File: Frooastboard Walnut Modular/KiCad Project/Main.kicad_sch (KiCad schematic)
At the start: 253 parts, among them M2 Frooastboard_MM2040

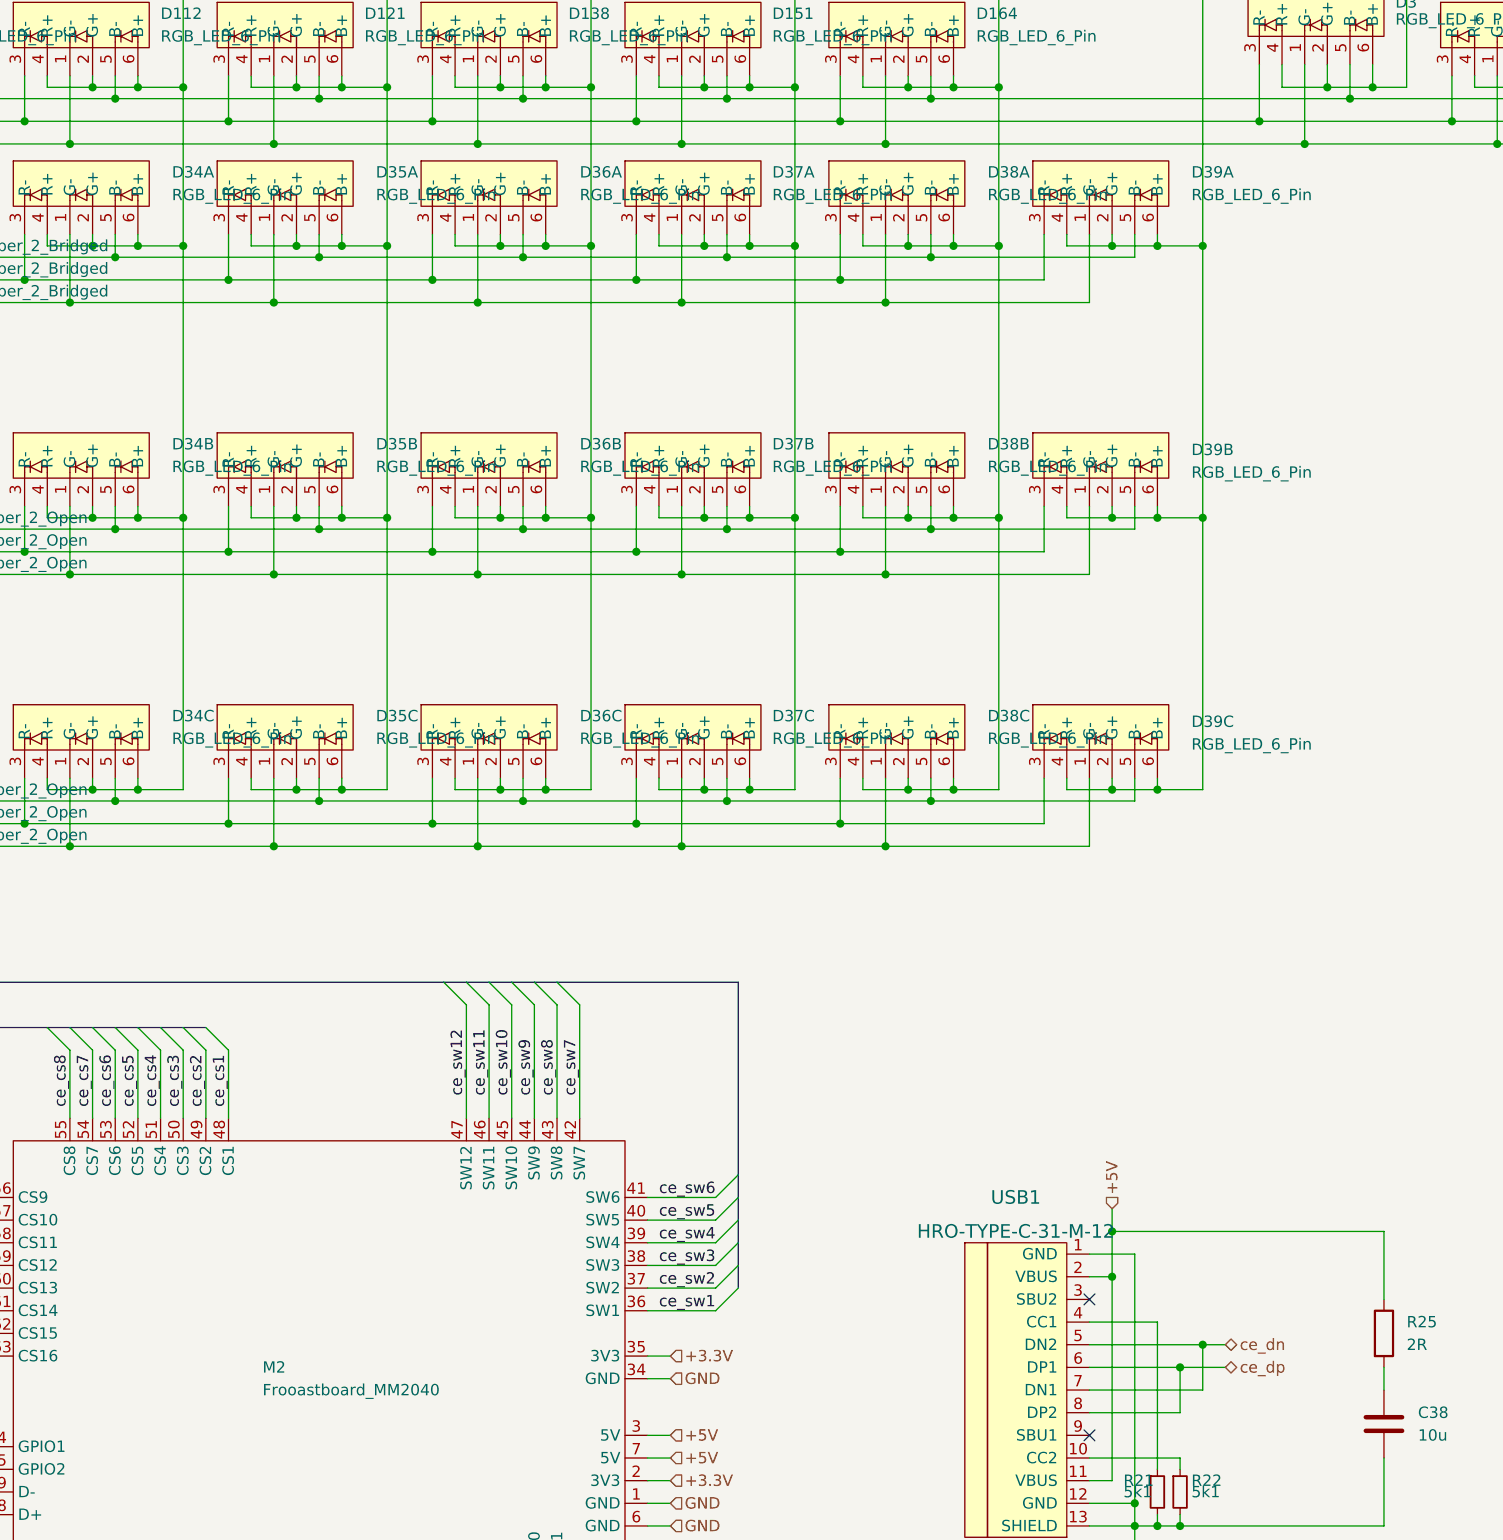
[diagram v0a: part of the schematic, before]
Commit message: update reference multi leds
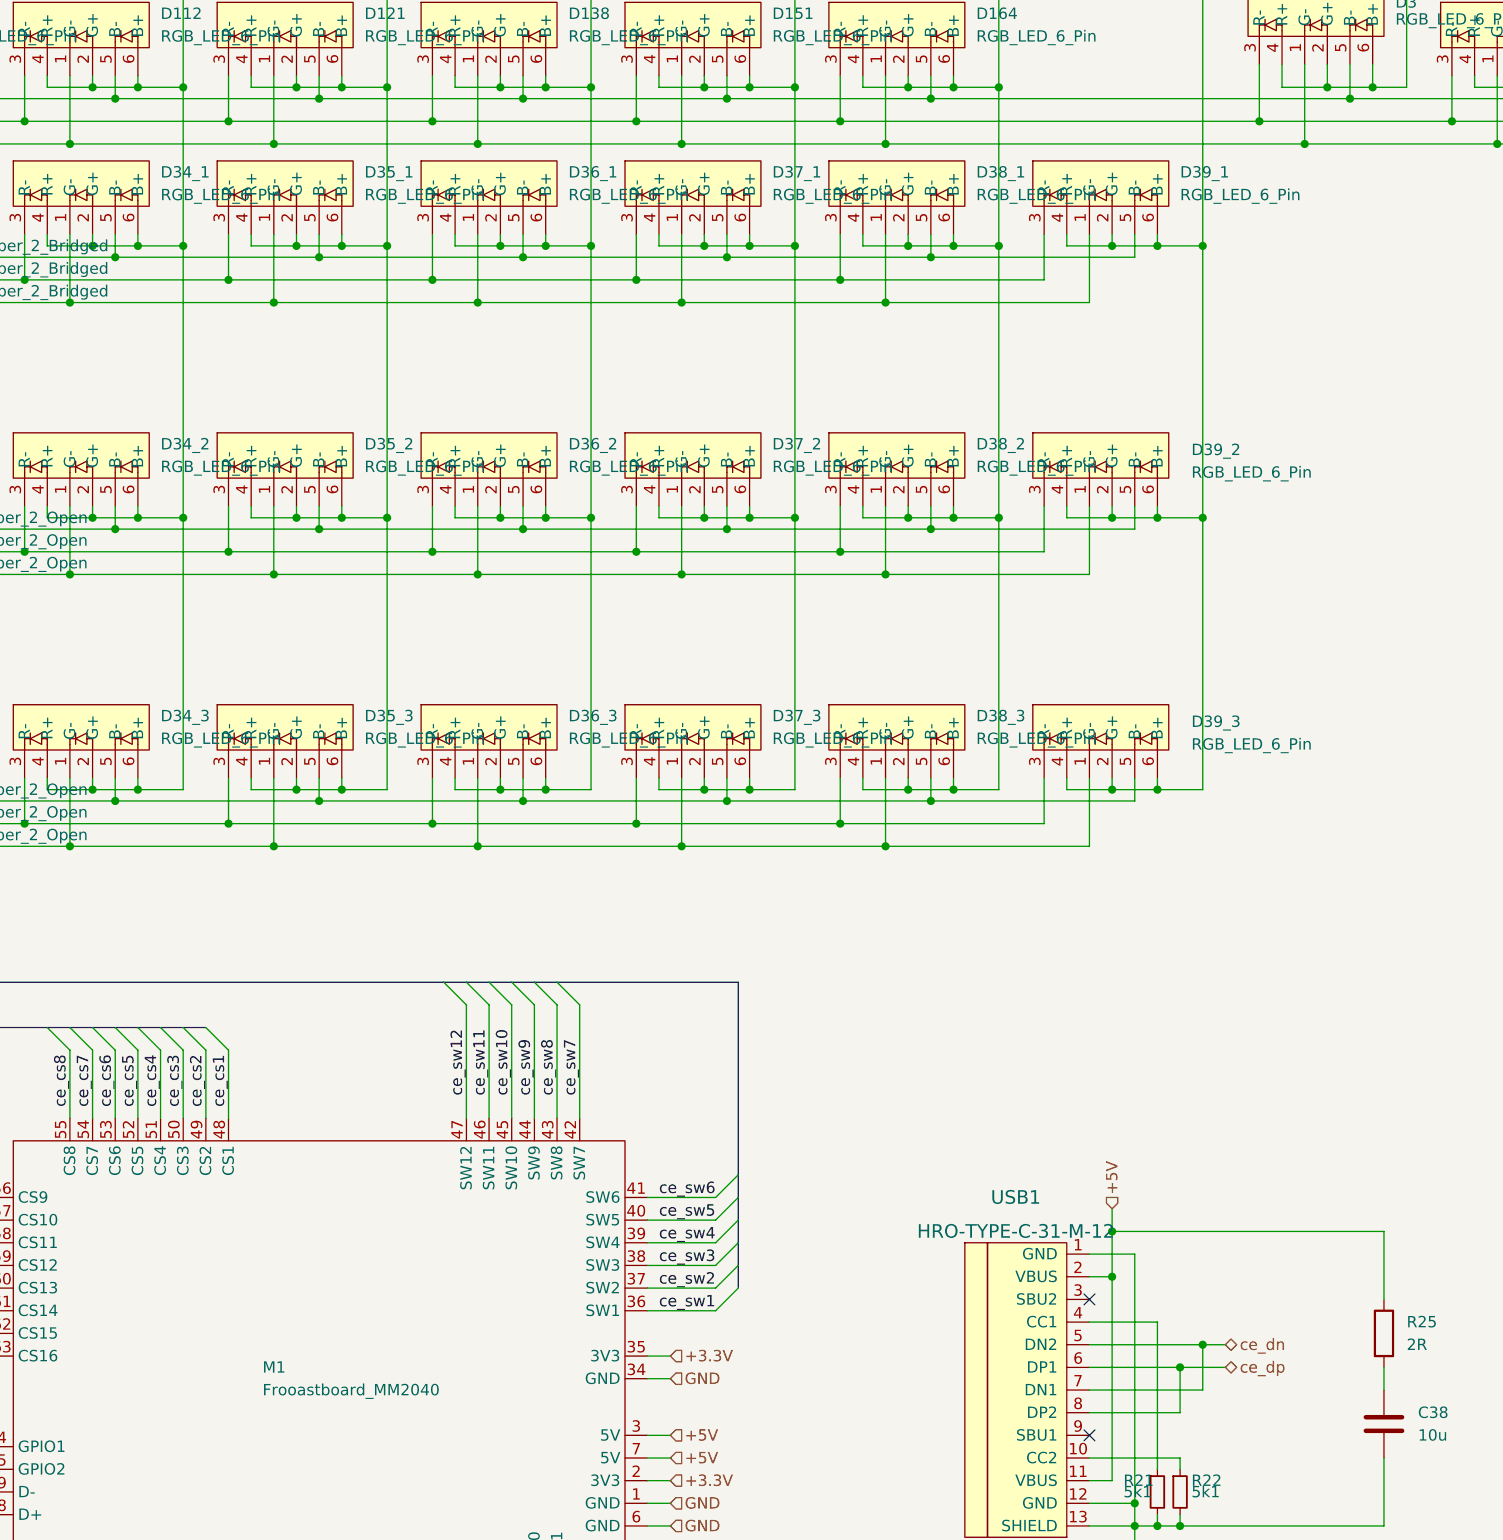
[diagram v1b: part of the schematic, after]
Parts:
- JP7, JP8, JP9: footprint (none) -> Jumper:SolderJumper-2_P1.3mm_Bridged_RoundedPad1.0x1.5mm
- renumbered D34A to D34_1, D34B to D34_2, D34C to D34_3, D35A to D35_1, D35B to D35_2, D35C to D35_3, D36A to D36_1, D36B to D36_2, D36C to D36_3, D37A to D37_1, D37B to D37_2, D37C to D37_3, D38A to D38_1, D38B to D38_2, D38C to D38_3, D39A to D39_1, D39B to D39_2, D39C to D39_3, M2 to M1

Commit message: idk some updates
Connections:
- no-connect marks 2 -> 4
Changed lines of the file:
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@@
   (junction (at 115.57 104.14) (diameter 0) (color 0 0 0 0)
   )
+  (no_connect (at 53.34 232.41))
   (no_connect (at 176.53 237.49))
+  (no_connect (at 53.34 234.95))
   (no_connect (at 176.53 222.25))
   (bus_entry (at 64.77 269.24) (size 2.54 -2.54)
@@
     )
     (pin "1")
+    (pin "10")
+    (pin "11")
     (pin "12")
     (pin "13")

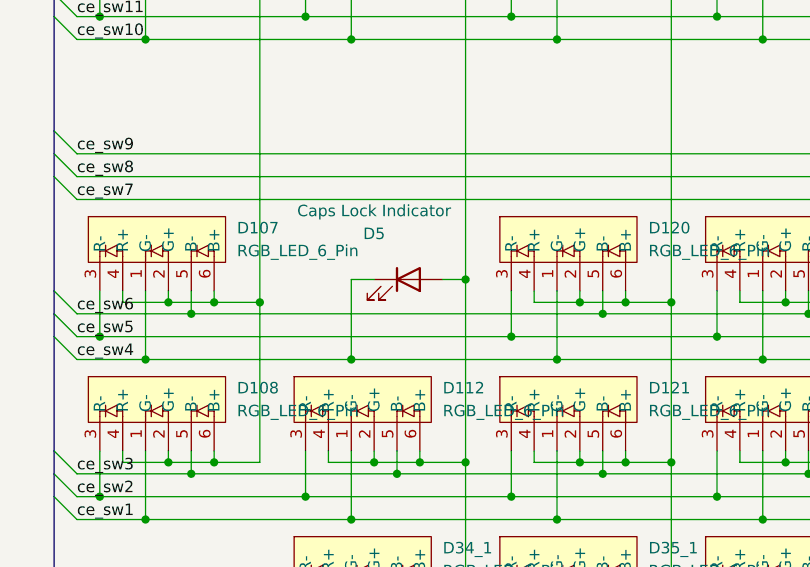
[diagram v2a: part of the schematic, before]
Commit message: update leds and diodes
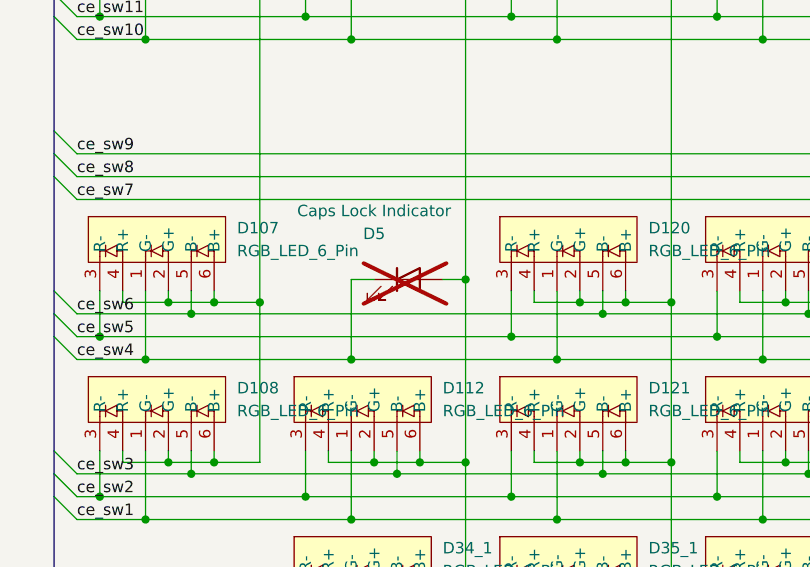
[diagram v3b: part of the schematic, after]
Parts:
- D5: now not fitted; now left out of the parts list
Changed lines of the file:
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@@
   )
   (symbol (lib_id "Device:LED") (at 68.58 66.04 0) (unit 1)
-    (in_bom yes) (on_board yes) (dnp no)
+    (in_bom no) (on_board no) (dnp yes)
     (property "Reference" "D5" (at 64.77 60.96 0)
       (effects (font (size 1.27 1.27)))

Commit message: some stuff
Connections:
- net ce_dn renamed ce_d-
- net ce_dp renamed ce_d+
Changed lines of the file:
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@@
     (effects (font (size 1.27 1.27)) (justify right))
   )
-  (hierarchical_label "ce_dp" (shape bidirectional) (at 50.8 246.38 180) (fields_autoplaced)
+  (hierarchical_label "ce_d+" (shape bidirectional) (at 50.8 246.38 180) (fields_autoplaced)
     (effects (font (size 1.27 1.27)) (justify right))
   )
@@
     (effects (font (size 1.27 1.27)) (justify right))
   )
-  (hierarchical_label "ce_dn" (shape bidirectional) (at 50.8 243.84 180) (fields_autoplaced)
+  (hierarchical_label "ce_d-" (shape bidirectional) (at 50.8 243.84 180) (fields_autoplaced)
     (effects (font (size 1.27 1.27)) (justify right))
   )
-  (hierarchical_label "ce_dp" (shape bidirectional) (at 191.77 229.87 0) (fields_autoplaced)
+  (hierarchical_label "ce_d+" (shape bidirectional) (at 191.77 229.87 0) (fields_autoplaced)
     (effects (font (size 1.27 1.27)) (justify left))
   )
@@
     (effects (font (size 1.27 1.27)) (justify left))
   )
-  (hierarchical_label "ce_dn" (shape bidirectional) (at 191.77 227.33 0) (fields_autoplaced)
+  (hierarchical_label "ce_d-" (shape bidirectional) (at 191.77 227.33 0) (fields_autoplaced)
     (effects (font (size 1.27 1.27)) (justify left))
   )

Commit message: fix errors
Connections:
- net ce_col9: now also D87.1 (K), D88.1 (K), D89.1 (K)
- net ce_row11: no longer D87.1 (K), D88.1 (K), D89.1 (K)
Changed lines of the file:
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@@
     (effects (font (size 1.27 1.27)) (justify left bottom))
   )
-  (label "ce_row11" (at 242.57 217.17 0) (fields_autoplaced)
+  (label "ce_col9" (at 242.57 217.17 0) (fields_autoplaced)
     (effects (font (size 1.27 1.27)) (justify left bottom))
   )
@@
     )
   )
-  (hierarchical_label "ce_row[0..11]" (shape input) (at 237.49 111.76 180) (fields_autoplaced)
+  (hierarchical_label "ce_row[0..9]" (shape input) (at 237.49 111.76 180) (fields_autoplaced)
     (effects (font (size 1.27 1.27)) (justify right))
   )
